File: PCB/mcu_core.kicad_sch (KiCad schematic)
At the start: 13 parts

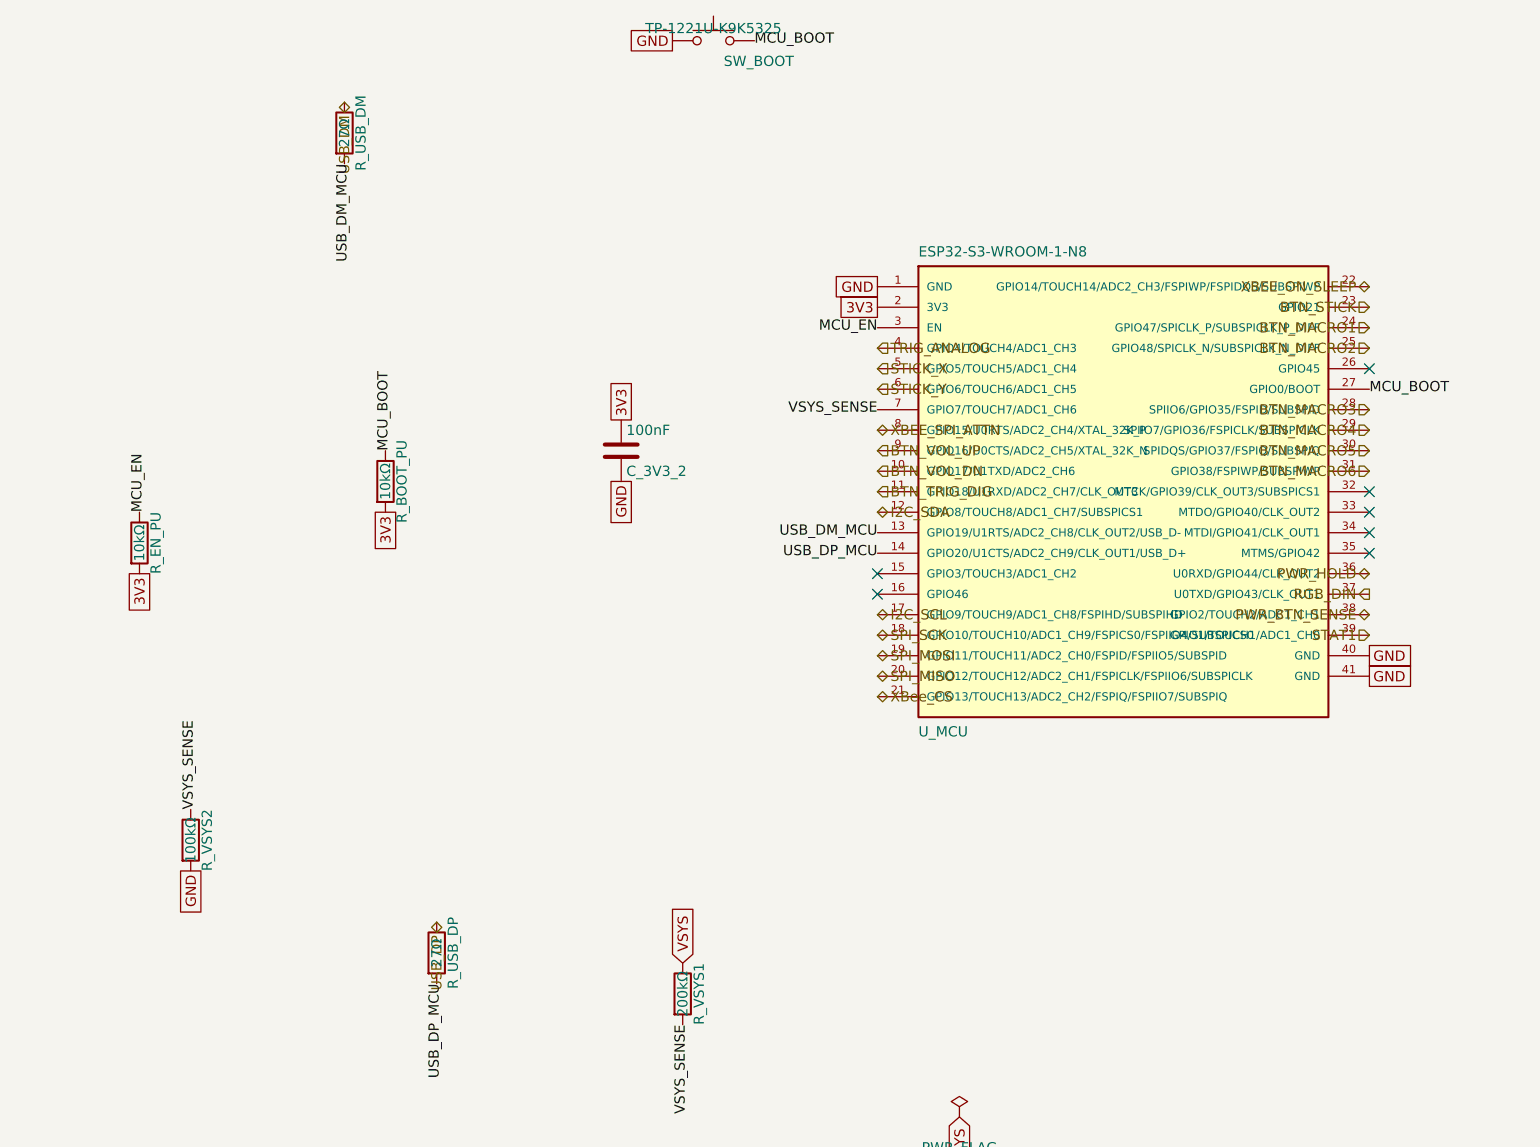
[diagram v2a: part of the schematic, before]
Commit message: cleanup: annotations and library updates
This is just a task to update the kicad libraries and annotations internally to get that clean ERC.
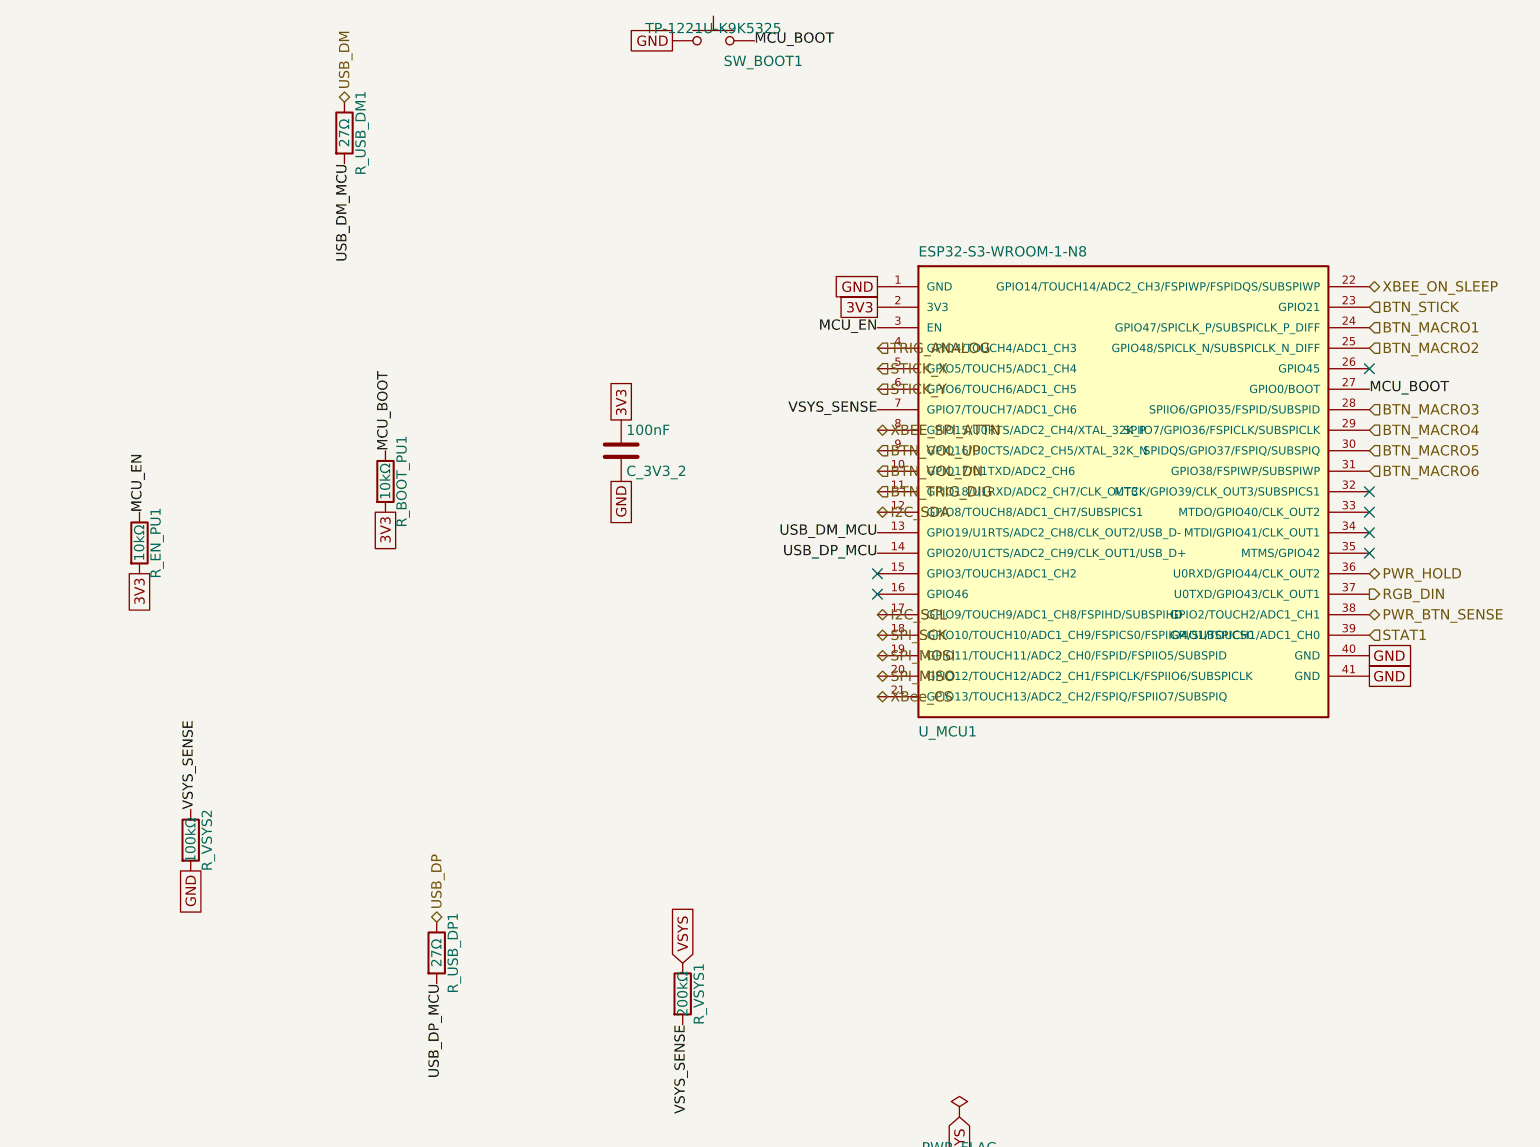
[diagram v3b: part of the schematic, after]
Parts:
- removed PF_3V3, PF_GND, PF_VSYS: PWR_FLAG, symbol power:PWR_FLAG
- U_MCU1: renamed from U_MCU; Description_1 (none) -> WiFi/BT module, integrated flash+crystal+antenna, ESP32-S3 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
- renumbered R_BOOT_PU to R_BOOT_PU1, R_EN_PU to R_EN_PU1, R_USB_DM to R_USB_DM1, R_USB_DP to R_USB_DP1, SW_BOOT to SW_BOOT1
